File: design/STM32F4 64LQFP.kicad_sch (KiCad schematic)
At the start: 15 parts, among them P9 SWD, U2 STM32F40X_LQFP64, X2 8MHz 10ppm

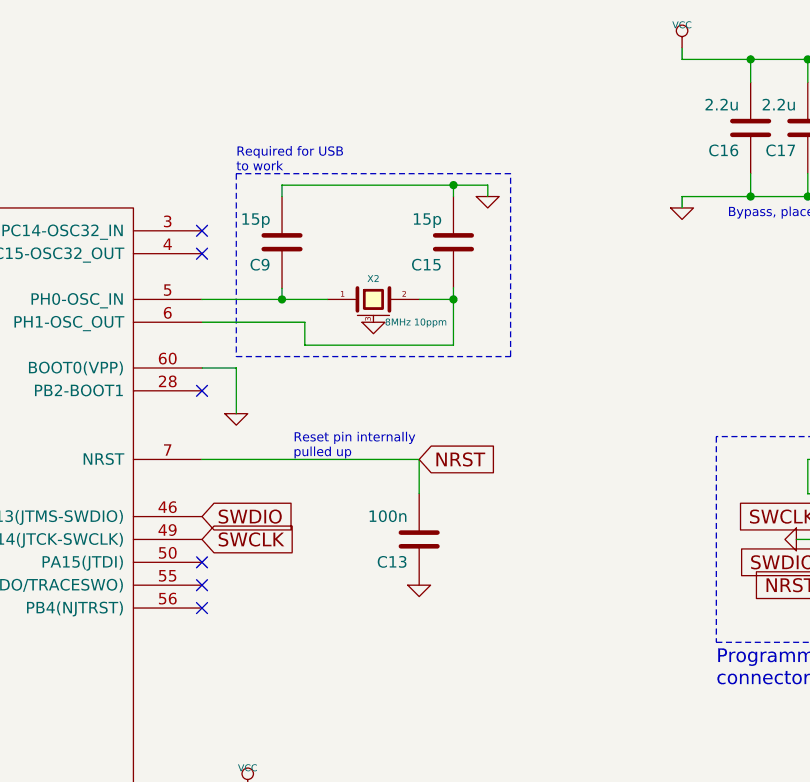
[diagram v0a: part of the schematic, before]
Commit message: added battery balancer
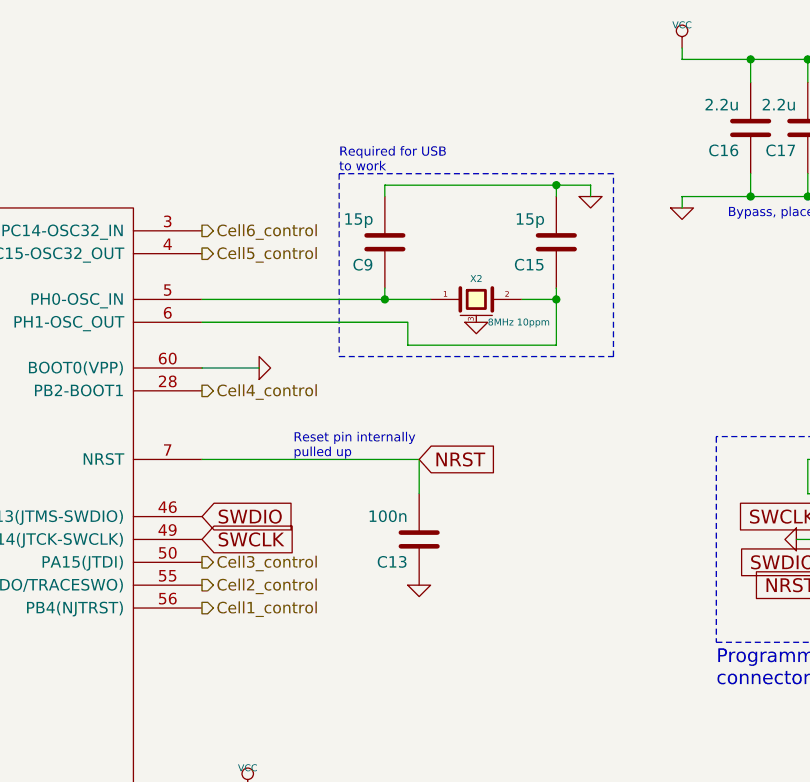
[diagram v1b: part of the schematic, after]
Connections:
- net Cell4_control: now reaches U2.28 (PB2-BOOT1)
- net Cell6_control: now reaches U2.3 (PC14-OSC32_IN)
- net Cell5_control: now reaches U2.4 (PC15-OSC32_OUT)
- net Cell3_control: now reaches U2.50 (PA15(JTDI))
- net Cell2_control: now reaches U2.55 (PB3(JTDO/TRACESWO))
- net Cell1_control: now reaches U2.56 (PB4(NJTRST))
- no-connect marks 7 -> 1
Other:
- moved on the sheet: C15, C9, X2

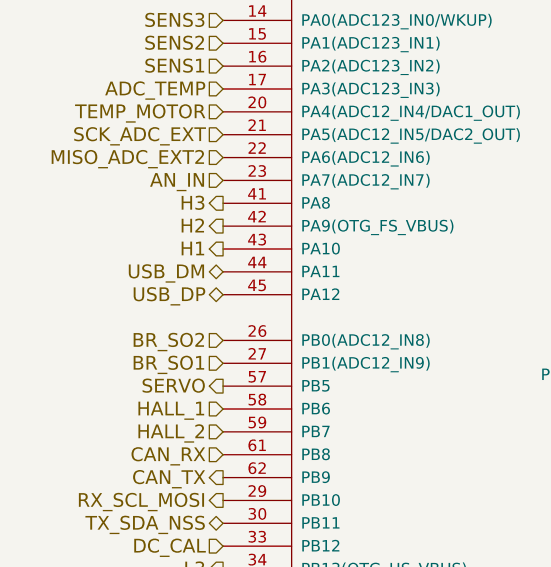
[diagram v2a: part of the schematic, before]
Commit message: added usb connector
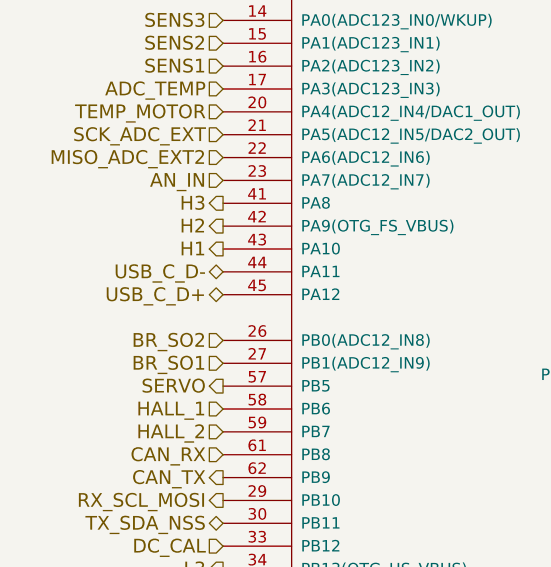
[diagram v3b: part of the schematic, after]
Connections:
- net USB_DM renamed USB_C_D-
- net USB_DP renamed USB_C_D+
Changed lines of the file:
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@@
+			"AAAAAAAAAAAAAAAAAAAAAAAAAAAAAAAAAAAAAAAAAAAAAAAAAAAAAAAAAAAAAAAAAAAAAAAAAAAA"
+			"AAAAAAAAAAAAAAAAAAAAAAAAAAAAAAAAAAAAAAAAAAAAAAAAAAAAAAAAAAAAAAAAAAAAAAAAAAAA"
+			"AAAAAAAAAAAAAAAAAAAAAAAAAAAAAAAAAAAAAAAAAAAAAAAAAAAAAAAAAAAAAAAAAAAAAAAAAAAA"
+			"AAAAAAAAAAAAAAAAAAAAAAAAAAAAAAAAAAAAAAAAAAAAAAAAAAAAAAAAAAAAAAAAAAAAAAAAAAAA"
+			"AAAAAAAAAAAAAAAAAAAAAAAAAAAAAAAAAAAAAAAAAAAAAAAAAAAAAAAAAAAAAAAAAAAAAAAAAAAA"
+			"AAAAAAAAAAAAAAAAAAAAAAAAAAAAAAAAAAAAAAAAAAAAAAAAAAAAAAAAAAAAAAAAAAAAAAAAAAAA"
+			"AAAAAAAAAAAAAAAAAAAAAAAAAAAAAAAAAAAAAAAAAAAAAAAAAAAAAAAAAAAAAAAAAAAAAAAAAAAA"
+			"AAAAAAAAAAAAAAAAAAAAAAAAAAAAAAAAAAAAAAAAAAAAAAAAAAAAAAAAAAAAAAAAAAAAAAAAAAAA"
+			"AAAAAAAAAAAAAAAAAAAAAAAAAAAAAAAAAAAAAAAAAAAAAAAAAAAAAAAAAAAAAAAAAAAAAAAAAAAA"
+			"AAAAAAAAAAAAAAAAAAAAAAAAAAAAAAAAAAAAAAAAAAAAAAAAAAAAAAAAAAAAAAAAAAAAAAAAAAAA"
+			"AAAAAAAAAAAAAAAAAAAAAAAAAAAAAAAAAAAAAAAAAAAAAAAAAAAAAAAAAAAAAAAAAAAAAAAAAAAA"
+			"AAAAAAAAAAAAAAAAAAAAAAAAAAAAAAAAAAAAAAAAAAAAAAAAAAAAAAAAAAAAAAAAAAAAAAAAAAAA"
+			"AAAAAAAAAAAAAAAAAAAAAAAAAAAAAAAAAAAAAAAAAAAAAAAAAAAAAAAAAAAAAAAAAAAAAAAAAAAA"
+			"AAAAAAAAAAAAAAAAAAAAAAAAAAAAAAAAAAAAAAAAAAAAAAAAAAAAAAAAAAAAAAAAAAAAAAAAAAAA"
+			"AAAAAAAAAAAAAAAAAAAAAAAAAAAAAAAAAAAAAAAAAAAAAAAAAAAAAAAAAAAAAAAAAAAAAAAAAAAA"
+			"AAAAAAAAAAAAAAAAAAAAAAAAAAAAAAAAAAAAAAAAAAAAAAAAAAAAAAAAAAAAAAAAAAAAAAAAAAAA"
+			"AAAAAAAAAAAAAAAAAAAAAAAAAAAAAAAAAAAAAAAAAAAAAAAAAAAAAAAAAAAAAAAAAAAAAAAAAAAA"
+			"AAAAAAAAAAAAAAAAAAAAAAAAAAAAAAAAAAAAAAAAAAAAAAAAAAAAAAAAAAAAAAAAAAAAAAAAAAAA"
 			"AAAAAAAAAAAAAAAAAAAAAAAAAAAAAAAAAAAAAAAAAAAAAAAAAAAAAAAAAAAAAAAAAAAAAAAAAAAA"
 			"AAAAAAAAAAAAAAAAAAAAAAAAAAAAAAAAAAAAAAAAAAAAAAAAAAAAAAAAAAAAAAAAAAAAAAAAAAAA"
@@
 			"AAAAAAAAAAAAAAAAAAAAAAAAAAAAAAAAAAAAAAAAAAAAAAAAAAAAAAAAAAAAAAAAAAAAAAAAAAAA"
 			"AAAAAAAAAAAAAAAAAAAAAAAAAAAAAAAAAAAAAAAAAAAAAAAAAAAAAAAAAAAAAAAAAAAAAAAAAAAA"
+			"AAAAAAAAAAAAAAAAAAAAAAAAAAAAAAAAAAAAAAAAAAAAAAAAAAAAAAAAAAAAAAAAAAAAAAAAAAAA"
+			"AAAAAAAAAAAAAAAAAAAAAAAAAAAAAAAAAAAAAAAAAAAAAAAAAAAAAAAAAAAAAAAAAAAAAAAAAAAA"
+			"AAAAAAAAAAAAAAAAAAAAAAAAAAAAAAAAAAAAAAAAAAAAAAAAAAAAAAAAAAAAAAAAAAAAAAAAAAAA"
+			"AAAAAAAAAAAAAAAAAAAAAAAAAAAAAAAAAAAAAAAAAAAAAAAAAAAAAAAAAAAAAAAAAAAAAAAAAAAA"
+			"AAAAAAAAAAAAAAAAAAAAAAAAAAAAAAAAAAAAAAAAAAAAAAAAAAAAAAAAAAAAAAAAAAAAAAAAAAAA"
+			"AAAAAAAAAAAAAAAAAAAAAAAAAAAAAAAAAAAAAAAAAAAAAAAAAAAAAAAAAAAAAAAAAAAAAAAAAAAA"
+			"AAAAAAAAAAAAAAAAAAAAAAAAAAAAAAAAAAAAAAAAAAAAAAAAAAAAAAAAAAAAAAAAAAAAAAAAAAAA"
+			"AAAAAAAAAAAAAAAAAAAAAAAAAAAAAAAAAAAAAAAAAAAAAAAAAAAAAAAAAAAAAAAAAAAAAAAAAAAA"
+			"AAAAAAAAAAAAAAAAAAAAAAAAAAAAAAAAAAAAAAAAAAAAAAAAAAAAAAAAAAAAAAAAAAAAAAAAAAAA"
+			"AAAAAAAAAAAAAAAAAAAAAAAAAAAAAAAAAAAAAAAAAAAAAAAAAAAAAAAAAAAAAAAAAAAAAAAAAAAA"
+			"AAAAAAAAAAAAAAAAAAAAAAAAAAAAAAAAAAAAAAAAAAAAAAAAAAAAAAAAAAAAAAAAAAAAAAAAAAAA"
+			"AAAAAAAAAAAAAAAAAAAAAAAAAAAAAAAAAAAAAAAAAAAAAAAAAAAAAAAAAAAAAAAAAAAAAAAAAAAA"
+			"AAAAAAAAAAAAAAAAAAAAAAAAAAAAAAAAAAAAAAAAAAAAAAAAAAAAAAAAAAAAAAAAAAAAAAAAAAAA"
+			"AAAAAAAAAAAAAAAAAAAAAAAAAAAAAAAAAAAAAAAAAAAAAAAAAAAAAAAAAAAAAAAAAAAAAAAAAAAA"
+			"AAAAAAAAAAAAAAAAAAAAAAAAAAAAAAAAAAAAAAAAAAAAAAAAAAAAAAAAAAAAAAAAAAAAAAAAAAAA"
+			"AAAAAAAAAAAAAAAAAAAAAAAAAAAAAAAAAAAAAAAAAAAAAAAAAAAAAAAAAAAAAAAAAAAAAAAAAAAA"
+			"AAAAAAAAAAAAAAAAAAAAAAAAAAAAAAAAAAAAAAAAAAAAAAAAAAAAAAAAAAAAAAAAAAAAAAAAAAAA"
+			"AAAAAAAAAAAAAAAAAAAAAAAAAAAAAAAAAAAAAAAAAAAAAAAAAAAAAAAAAAAAAAAAAAAAAAAAAAAA"
 			"AAAAAA=="
 		)
@@
 		)
 	)
-	(hierarchical_label "USB_DP"
+	(hierarchical_label "USB_C_D+"
 		(shape bidirectional)
 		(at 114.3 74.93 180)
@@
 		)
 	)
-	(hierarchical_label "USB_DM"
+	(hierarchical_label "USB_C_D-"
 		(shape bidirectional)
 		(at 114.3 72.39 180)

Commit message: added documentation
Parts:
- C10: The code for order (none) -> CL10B225KP8NNNC; Значение (none) -> 2.2 мкФ; Наименование (none) -> Конденсатор керамический 2.2 мкФ 0603; Обозначение (none) -> C; Позиционное обозначение (none) -> C10
- C11: The code for order (none) -> CL10B225KP8NNNC; Значение (none) -> 2.2 мкФ; Наименование (none) -> Конденсатор керамический 2.2 мкФ 0603; Обозначение (none) -> C; Позиционное обозначение (none) -> C11
- C12: The code for order (none) -> CL10B225KP8NNNC; Значение (none) -> 2.2 мкФ; Наименование (none) -> Конденсатор керамический 2.2 мкФ 0603; Обозначение (none) -> C; Позиционное обозначение (none) -> C12
- C13: The code for order (none) -> C1206C104K5RAC7210; Значение (none) -> 100 нФ; Наименование (none) -> Конденсатор керамический 100 нФ 0603; Обозначение (none) -> C; Позиционное обозначение (none) -> C13
- C14: The code for order (none) -> CL10B225KP8NNNC; Значение (none) -> 2.2 мкФ; Наименование (none) -> Конденсатор керамический 2.2 мкФ 0603; Обозначение (none) -> C; Позиционное обозначение (none) -> C14
- C15: The code for order (none) -> CL10C150JB8NNNC; Значение (none) -> 15 пФ; Наименование (none) -> Конденсатор керамический 15 пФ 0603; Обозначение (none) -> C; Позиционное обозначение (none) -> C15
- C16: The code for order (none) -> CL10B225KP8NNNC; Значение (none) -> 2.2 мкФ; Наименование (none) -> Конденсатор керамический 2.2 мкФ 0603; Обозначение (none) -> C; Позиционное обозначение (none) -> C16
- C17: The code for order (none) -> CL10B225KP8NNNC; Значение (none) -> 2.2 мкФ; Наименование (none) -> Конденсатор керамический 2.2 мкФ 0603; Обозначение (none) -> C; Позиционное обозначение (none) -> C17
- C18: The code for order (none) -> CL10B225KP8NNNC; Значение (none) -> 2.2 мкФ; Наименование (none) -> Конденсатор керамический 2.2 мкФ 0603; Обозначение (none) -> C; Позиционное обозначение (none) -> C18
- C19: The code for order (none) -> CL10B225KP8NNNC; Значение (none) -> 2.2 мкФ; Наименование (none) -> Конденсатор керамический 2.2 мкФ 0603; Обозначение (none) -> C; Позиционное обозначение (none) -> C19
- C20: The code for order (none) -> CL10B225KP8NNNC; Значение (none) -> 2.2 мкФ; Наименование (none) -> Конденсатор керамический 2.2 мкФ 0603; Обозначение (none) -> C; Позиционное обозначение (none) -> C20
- C9: The code for order (none) -> CL10C150JB8NNNC; Значение (none) -> 15 пФ; Наименование (none) -> Конденсатор керамический 15 пФ 0603; Обозначение (none) -> C; Позиционное обозначение (none) -> C9
- P9: The code for order (none) -> NDSR-02-V; Значение (none) -> SWD; Наименование (none) -> Разъём питания JST-6; Обозначение (none) -> XS; Позиционное обозначение (none) -> P9
- U2: The code for order (none) -> STM32F401RBT6TR; Значение (none) -> STM32F40X; Наименование (none) -> Микроконтроллер STM32F40X LQFP64; Обозначение (none) -> DD; Позиционное обозначение (none) -> U2
- X2: The code for order (none) -> NX5032GA-8.000M-STD-CSU-1; Значение (none) -> 8 МГц; Наименование (none) -> Кварцевый резонатор 8 МГц 10ppm; Обозначение (none) -> ZQ; Позиционное обозначение (none) -> X2
